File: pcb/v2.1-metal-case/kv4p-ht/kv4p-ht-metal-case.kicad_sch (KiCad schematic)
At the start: 83 parts, among them J1 Antenna, J5 USB-C Socket, Q1 SS8050, Q2 SS8050, Q3 AO3400A, SW1 Program, SW2 Program, SW3 Reset, SW4 Program, U1 DRA/SA818, U2 AZ1117H-3.3TRG1, U4 CP2102N-A02-GQFN24, U5 ESP32-WROOM-32E-N4

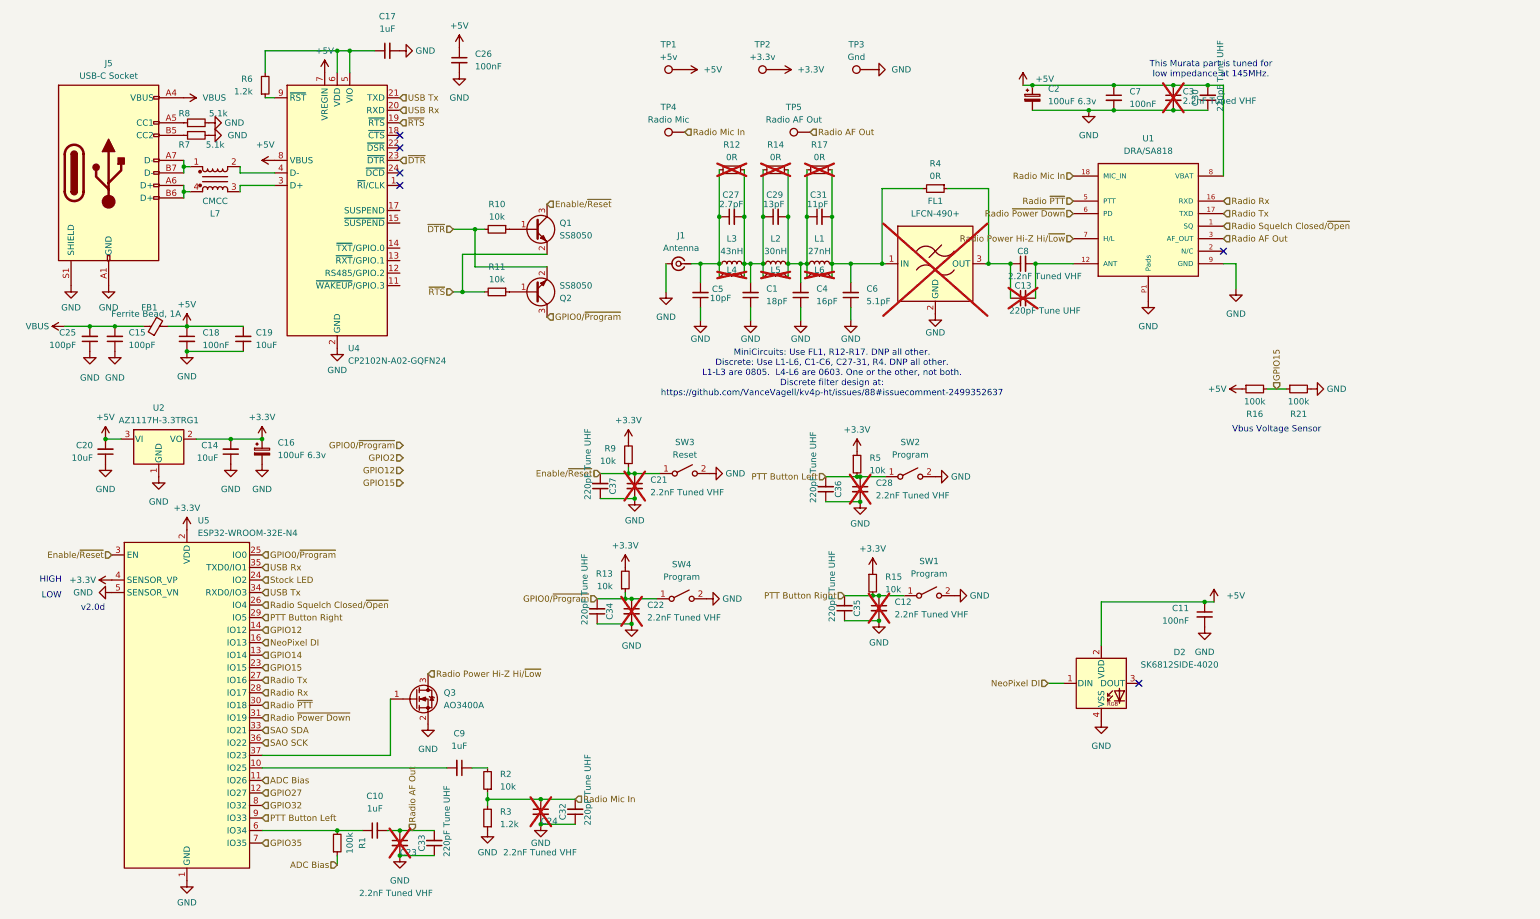
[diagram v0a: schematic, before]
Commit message: More work on v2.1: UHF support, USB CMCC, 80x50x20mm case. #22
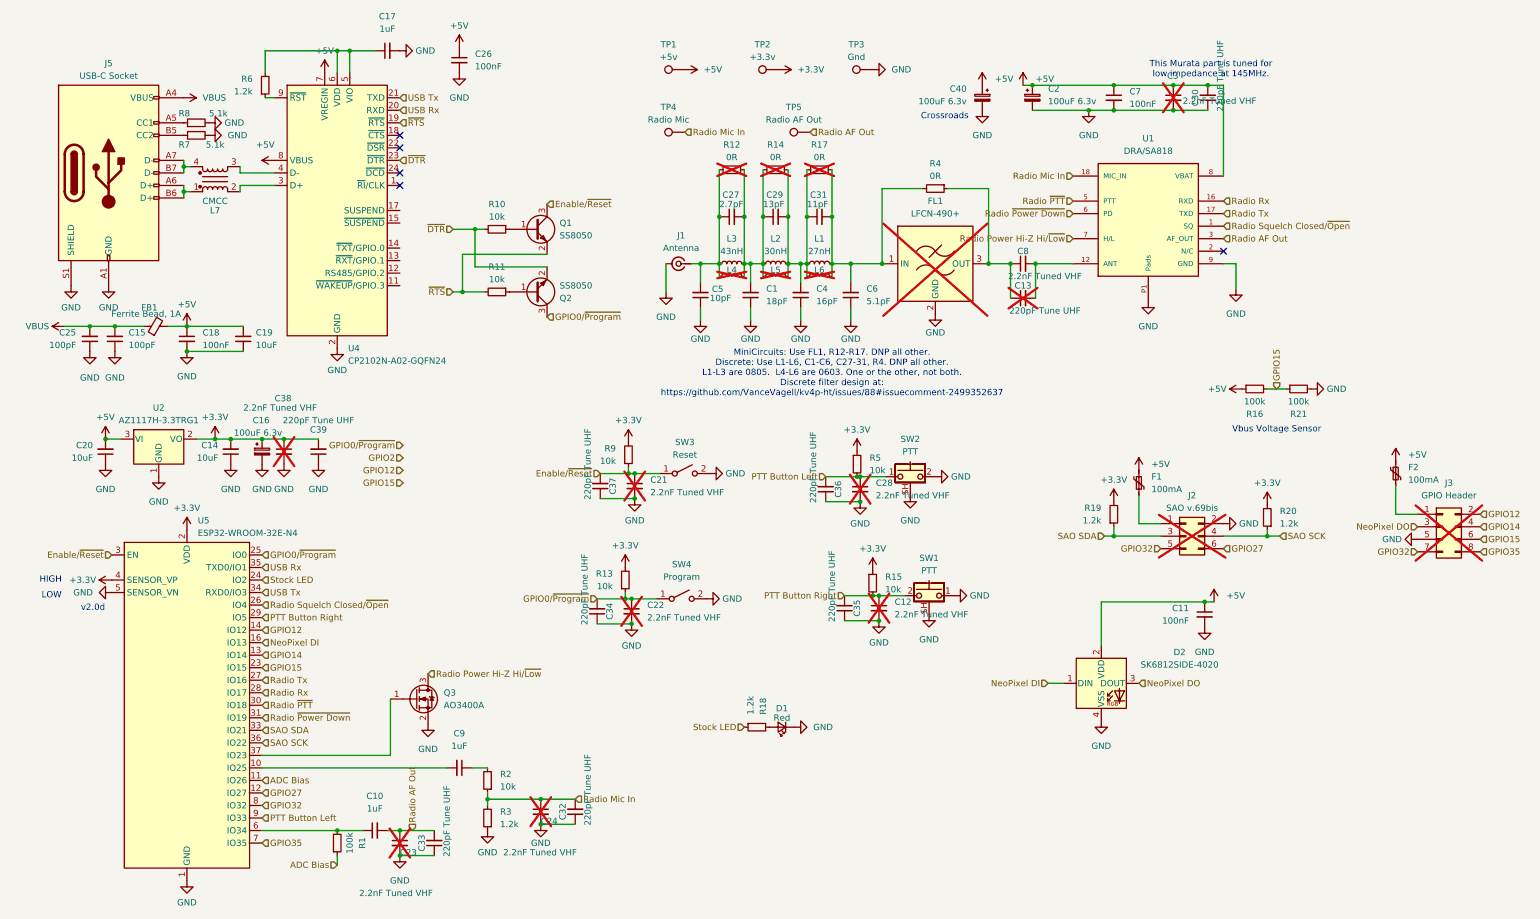
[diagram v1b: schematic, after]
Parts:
- removed SW1, SW2: Program, Button_Switch_SMD:SW_SPST_TL3342, symbol Switch:SW_SPST
- added C38: 2.2nF Tuned VHF, Capacitor_SMD:C_0603_1608Metric, symbol Device:C_Small
- added C39: 220pF Tune UHF, Capacitor_SMD:C_0603_1608Metric, symbol Device:C_Small
- added C40: 100uF 6.3v, Capacitor_Tantalum_SMD:CP_EIA-3528-21_Kemet-B, symbol Device:C_Polarized_Small
- added D1: Red, LED_SMD:LED_0603_1608Metric, symbol Device:LED_Small
- added F1, F2: 100mA, Fuse:Fuse_0603_1608Metric, symbol Device:Polyfuse_Small
- added J2: SAO v.69bis, Connector_PinHeader_2.54mm:PinHeader_2x03_P2.54mm_Vertical_SMD, symbol Connector_Generic:Conn_02x03_Odd_Even
- added J3: GPIO Header, Connector_PinHeader_2.54mm:PinHeader_2x04_P2.54mm_Vertical_SMD, symbol Connector_Generic:Conn_02x04_Odd_Even
- added R18, R19, R20: 1.2k, Resistor_SMD:R_0603_1608Metric, symbol Device:R_Small
- added SW1, SW2: PTT, kv4p-ht:SW-Push-SPST-Horizontal-C455252, symbol Switch:SW_Push_Shielded
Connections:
- net +3.3V: now also C38.1, C39.2, R19.2, R20.2
- net +5V: now also C40.1, F1.1, F2.1
- net GND: now also C38.2, C39.1, C40.2, D1.1 (K), J2.2 (Pin_2), J3.5 (Pin_5), SW1.1, SW1.SH (B), SW2.2, SW2.SH (B)
- net GPIO12: now also J3.2 (Pin_2)
- net GPIO14: now also J3.4 (Pin_4)
- net GPIO15: now also J3.6 (Pin_6)
- net GPIO27: now also J2.6 (Pin_6)
- net GPIO32: now also J2.5 (Pin_5), J3.7 (Pin_7)
- net GPIO35: now also J3.8 (Pin_8)
- net PTT Button Left: now also SW2.1
- net PTT Button Right: now also SW1.2
- net SAO SCK: now also J2.4 (Pin_4), R20.1
- net SAO SDA: now also J2.3 (Pin_3), R19.1
- net Stock LED: now also R18.1
- net at U4.3 (D+): now also L7.2; no longer L7.3
- net at U4.4 (D-): now also L7.3; no longer L7.2
- net at J5.A6 (D+), J5.B6 (D+): now also L7.1; no longer L7.4
- net at J5.A7 (D-), J5.B7 (D-): now also L7.4; no longer L7.1
- net NeoPixel DO: now reaches D2.3 (DOUT)
- net NeoPixel DO: now also J3.3 (Pin_3)
- new net: F1.2, J2.1 (Pin_1)
- new net: D1.2 (A), R18.2
- new net: F2.2, J3.1 (Pin_1)
- no-connect marks 6 -> 5
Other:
- note added: "Crossroads"

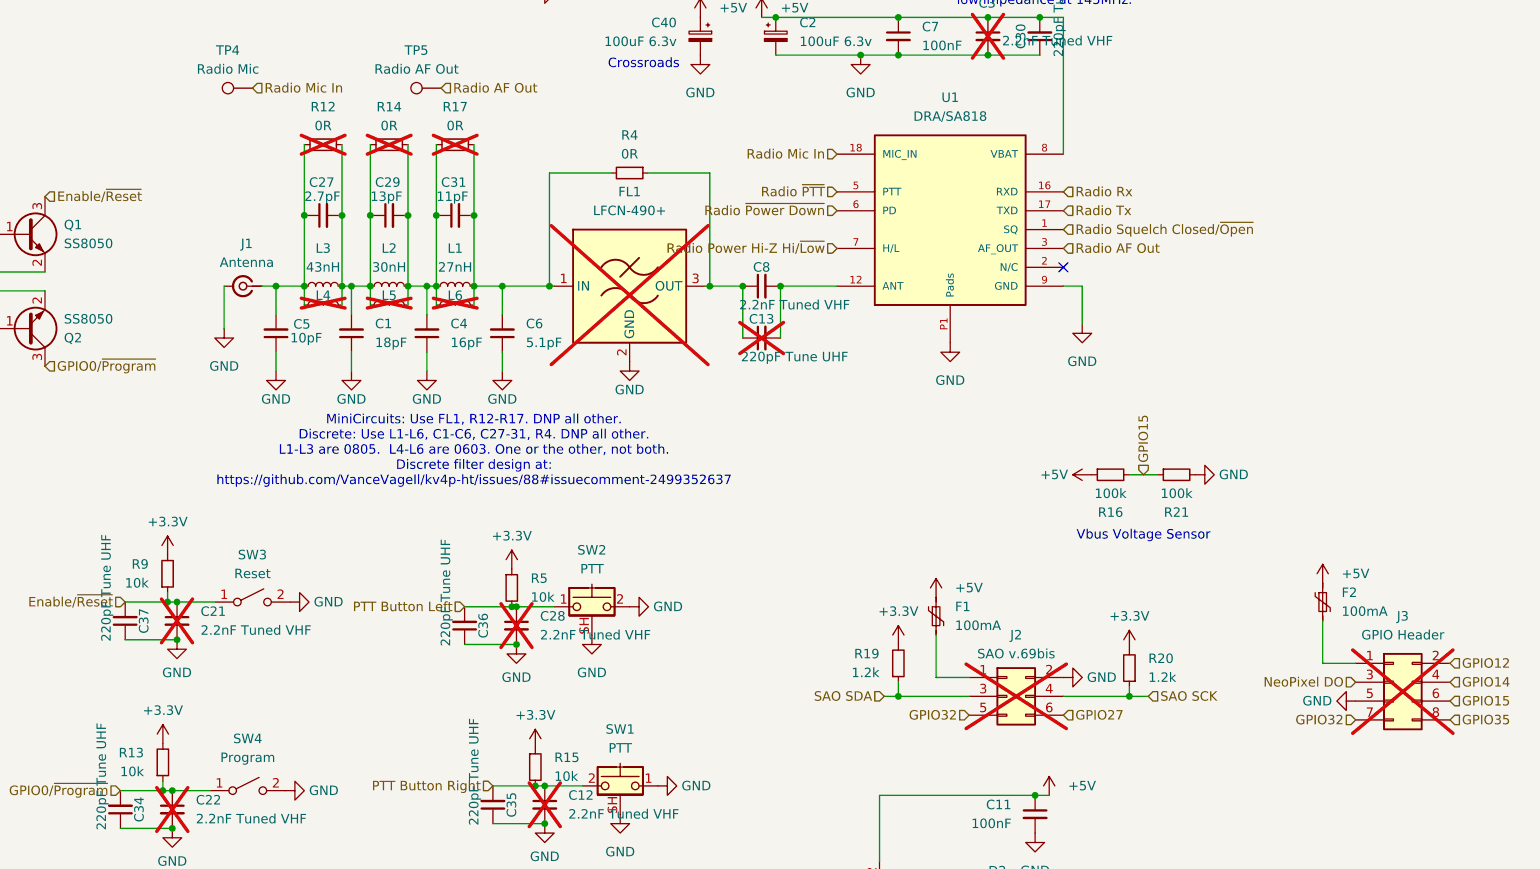
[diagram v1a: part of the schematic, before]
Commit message: v2.1b as ordered 2025-04-17. VHF and UHF #22. SAO headers. PTT buttons. User LED.
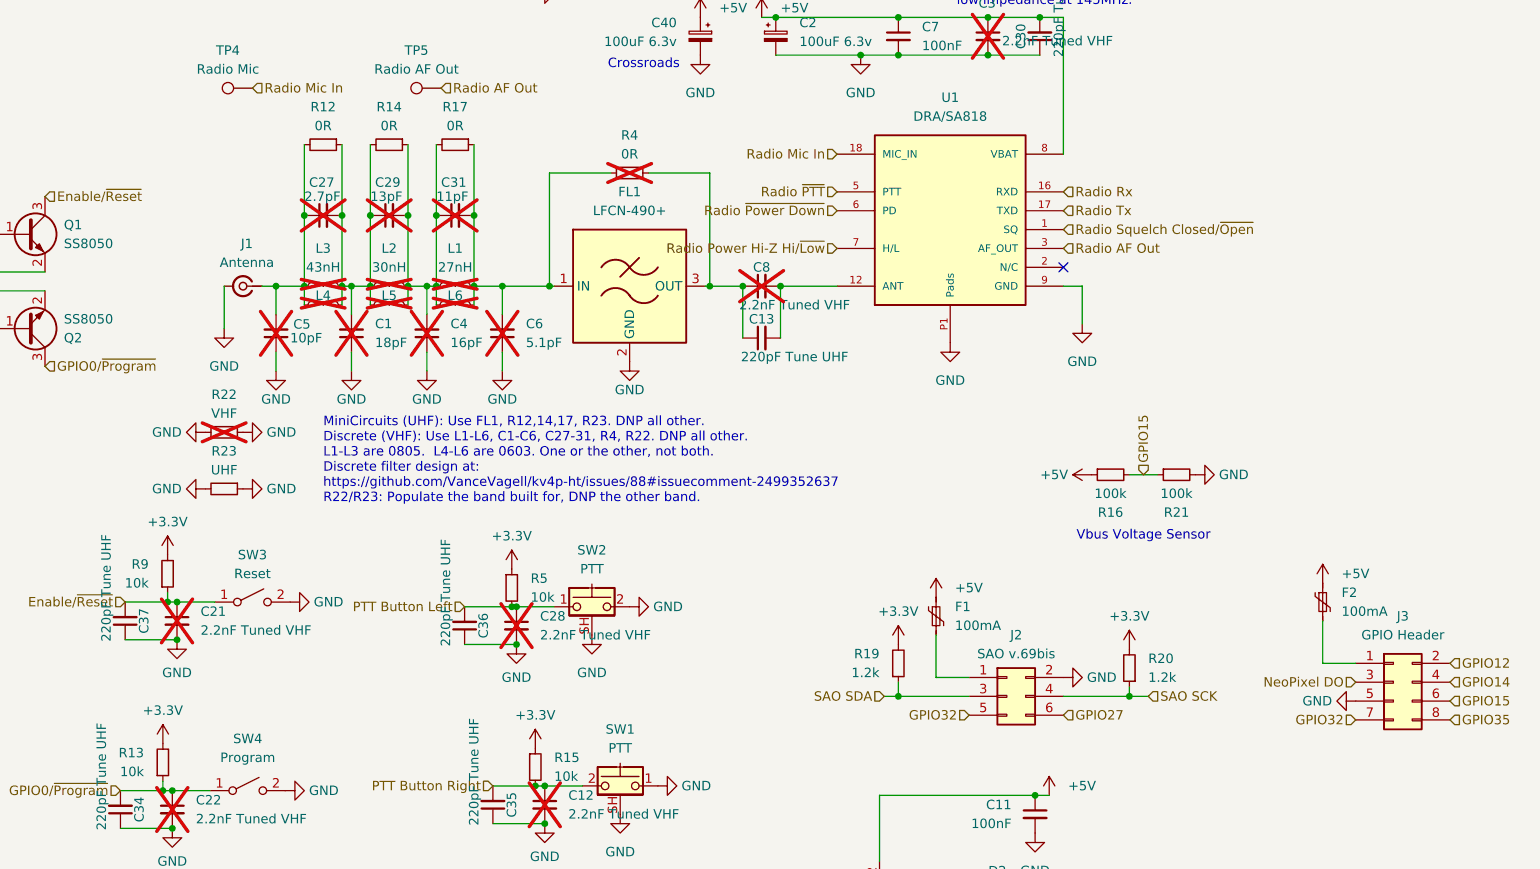
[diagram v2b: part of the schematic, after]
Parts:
- added R22: VHF, Resistor_SMD:R_1206_3216Metric, symbol Device:R_Small
- added R23: UHF, Resistor_SMD:R_1206_3216Metric, symbol Device:R_Small
- C1, C27, C29, C31, C4, C5, C6, C8, L1, L2, L3, R4: now not fitted
- C13, FL1, R12, R14, R17: now fitted
- C16, C2, C40: FT Rotation Offset (none) -> 180
- D2: FT Position Offset (none) -> 0.0,1.397; LCSC C2890037 -> C5378721
- J1: footprint Connector_Coaxial:SMA_Amphenol_901-143_Horizontal -> Libraries:Conn_SMA_Close-to-board-edge; FT Rotation Offset (none) -> 90
- J2, J3: FT Rotation Offset (none) -> 90; now fitted
- J5: FT Position Offset (none) -> 0.0,1.3335
- SW1, SW2: FT Position Offset (none) -> 0.0,-0.3175; FT Rotation Offset (none) -> 180
- U4: FT Rotation Offset (none) -> -90
- U5: FT Position Offset (none) -> 0.0,-0.77; FT Rotation Offset (none) -> -90
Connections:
- net GND: now also R22.1, R22.2, R23.1, R23.2
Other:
- note added: "MiniCircuits (UHF): Use FL1, R12,14,17, R23. DNP all other. Discrete (VHF): Use L1-L6, C1-C6, C27-31, R4, R22. DNP all other. L1-L3 are 0805. L4-L6 are 0603. One or the other, not both. Discrete filter design at: https://github.com/VanceVagell/kv4p-ht/issues/88#issuecomment-2499352637 R22/R23: Populate the band built for, DNP the other band."
- note removed: "MiniCircuits: Use FL1, R12-R17. DNP all other. Discrete: Use L1-L6, C1-C6, C27-31, R4. DNP all other. L1-L3 are 0805. L4-L6 are 0603. One or the other, not both. Discrete filter design at: https://github.com/VanceVagell/kv4p-ht/issues/88#issuecomment-2499352637"
